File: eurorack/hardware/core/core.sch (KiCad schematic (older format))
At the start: 48 parts, among them J1 ConnNW, J2 ConnSW, J3 ConnNE, J4 ConnSE, J5 Power, J6 SWD, SW1 Reset, SW2 Boot0, U1 STM32F427VGT6, U2 TLV320AIC23BPW, U3 LM1117F-3.3, U4 LM4040C10IDBZR, Y1 Crystal

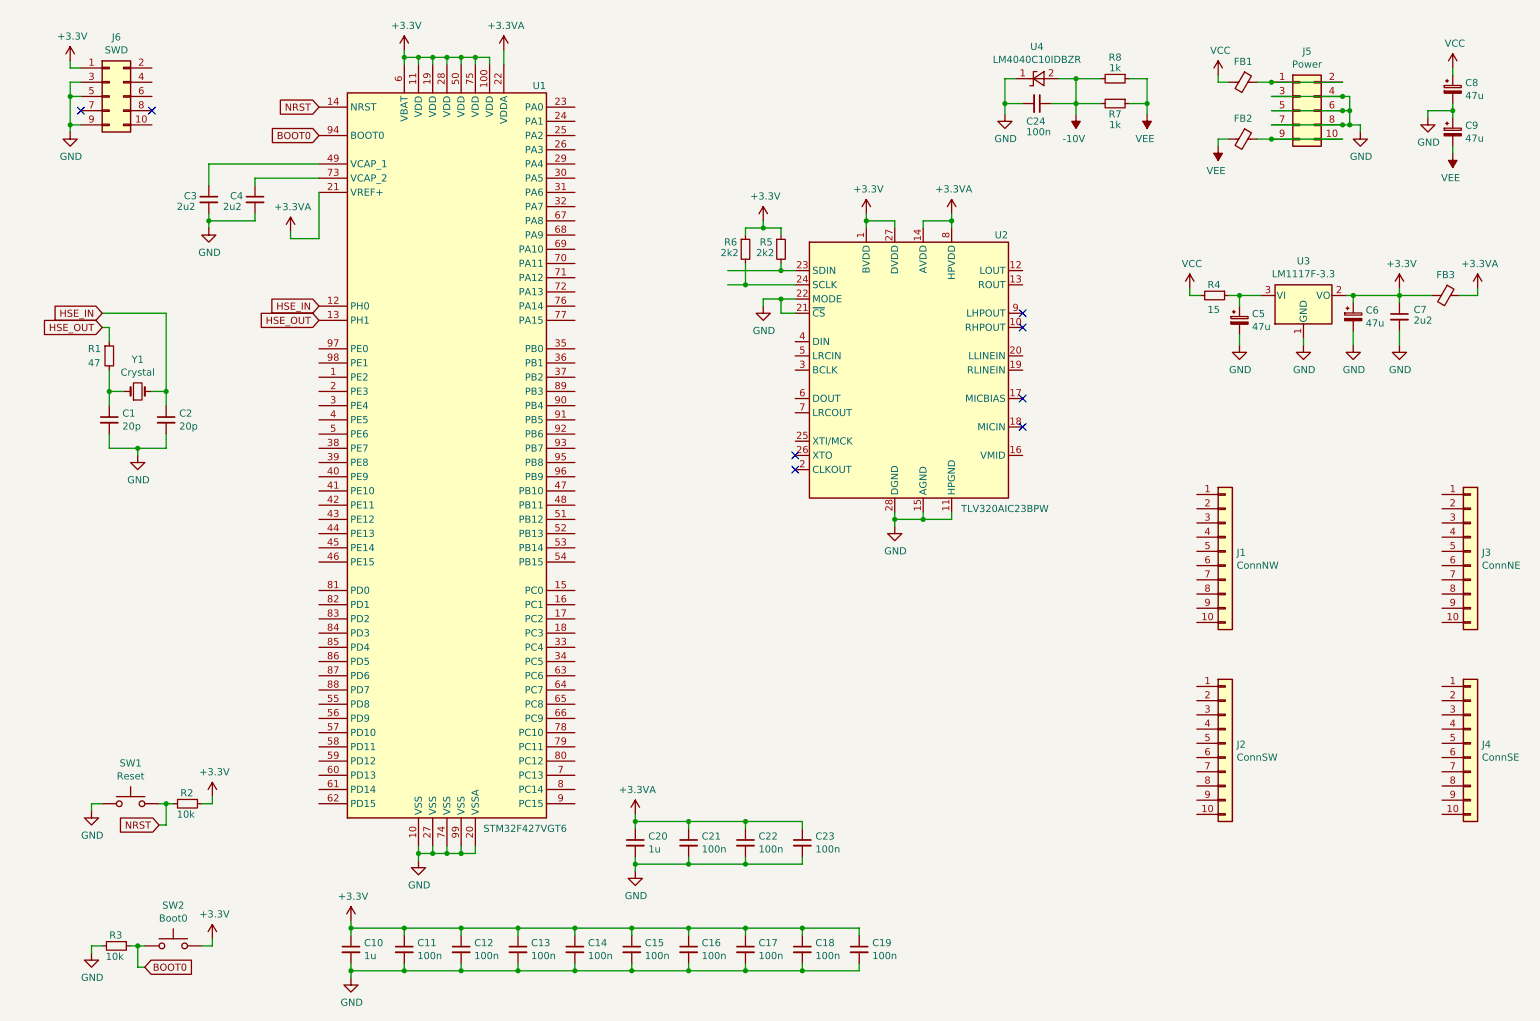
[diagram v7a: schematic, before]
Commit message: Connect DAC and JTAG
Signed-off-by: Petr Horacek <hrck@protonmail.com>
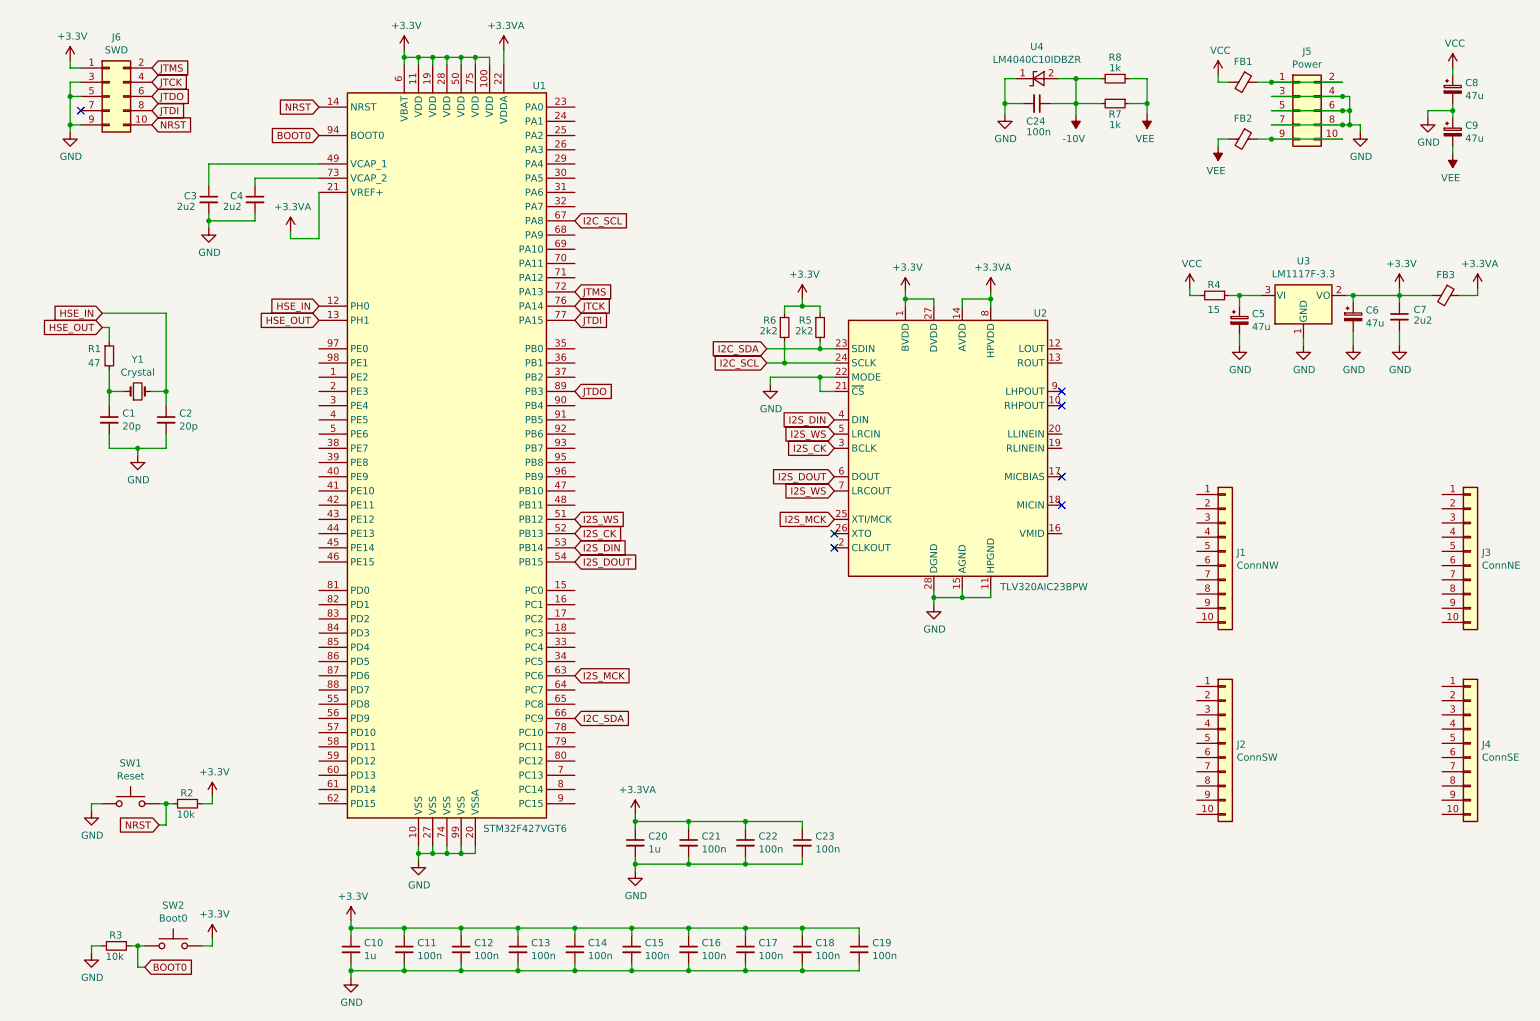
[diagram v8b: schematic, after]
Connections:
- net NRST: now also J6.10 (Pin_10)
- net I2S_WS: now reaches U1.51 (PB12)
- net I2S_WS: now also U2.5 (LRCIN), U2.7 (LRCOUT)
- net I2S_CK: now reaches U1.52 (PB13)
- net I2S_CK: now also U2.3 (BCLK)
- net I2S_DIN: now reaches U1.53 (PB14)
- net I2S_DIN: now also U2.4 (DIN)
- net I2S_DOUT: now reaches U1.54 (PB15)
- net I2S_DOUT: now also U2.6 (DOUT)
- net I2S_MCK: now reaches U1.63 (PC6)
- net I2S_MCK: now also U2.25 (XTI/MCK)
- net I2C_SDA: now reaches U1.66 (PC9)
- net I2C_SDA: now also R5.2, U2.23 (SDIN)
- net I2C_SCL: now reaches U1.67 (PA8)
- net I2C_SCL: now also R6.2, U2.24 (SCLK)
- net JTMS: now reaches U1.72 (PA13)
- net JTMS: now also J6.2 (Pin_2)
- net JTCK: now reaches U1.76 (PA14)
- net JTCK: now also J6.4 (Pin_4)
- net JTDI: now reaches U1.77 (PA15)
- net JTDI: now also J6.8 (Pin_8)
- net JTDO: now reaches U1.89 (PB3)
- net JTDO: now also J6.6 (Pin_6)
- no-connect marks 8 -> 7
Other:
- moved on the sheet: R5, R6, U2
